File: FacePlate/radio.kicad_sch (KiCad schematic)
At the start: 4 parts, among them U3 SX1280

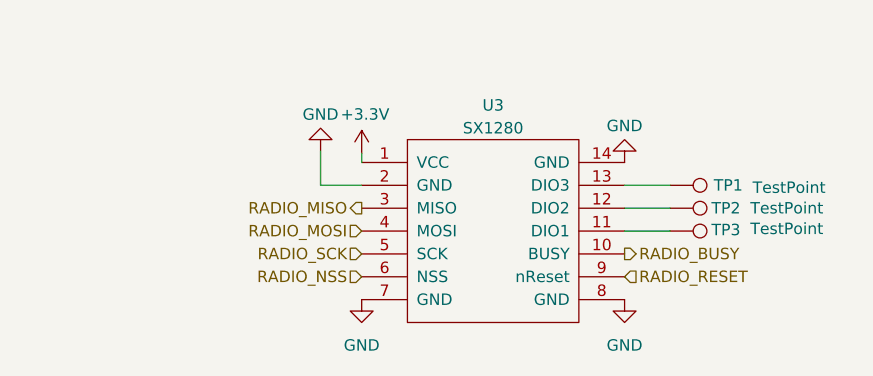
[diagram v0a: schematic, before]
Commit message: WIP Buck for Faceplate
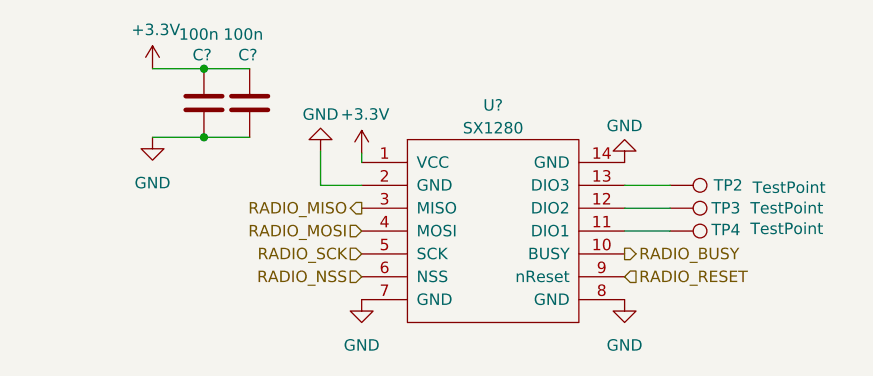
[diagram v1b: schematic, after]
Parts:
- added C? (x2): 100n, Capacitor_SMD:C_0603_1608Metric, symbol Device:C
- TP2: renamed from TP1; footprint (none) -> TestPoint:TestPoint_Pad_D1.0mm
- TP3: renamed from TP2; footprint (none) -> TestPoint:TestPoint_Pad_D1.0mm
- TP4: renamed from TP3; footprint (none) -> TestPoint:TestPoint_Pad_D1.0mm
- U?: renamed from U3; footprint BlueKitchen:E28-2G4M12S-SX1280 -> SX1280:E28-2G4M12S-SX1280
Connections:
- net +3.3V: now also C?.1, C?.1
- net GND: now also C?.2, C?.2

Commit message: Finalize faceplate
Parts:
- C?: LCSC C307341 -> C14663
- C?: LCSC C307340 -> C14663
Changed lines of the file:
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@@
       (effects (font (size 1.27 1.27)) hide)
     )
-    (property "LCSC" "C307341" (at 114.3 84.836 0)
+    (property "LCSC" "C14663" (at 114.3 84.836 0)
       (effects (font (size 1.27 1.27)) (justify left) hide)
     )
@@
       (effects (font (size 1.27 1.27)) hide)
     )
-    (property "LCSC" "C307340" (at 109.22 84.836 0)
+    (property "LCSC" "C14663" (at 109.22 84.836 0)
       (effects (font (size 1.27 1.27)) (justify left) hide)
     )

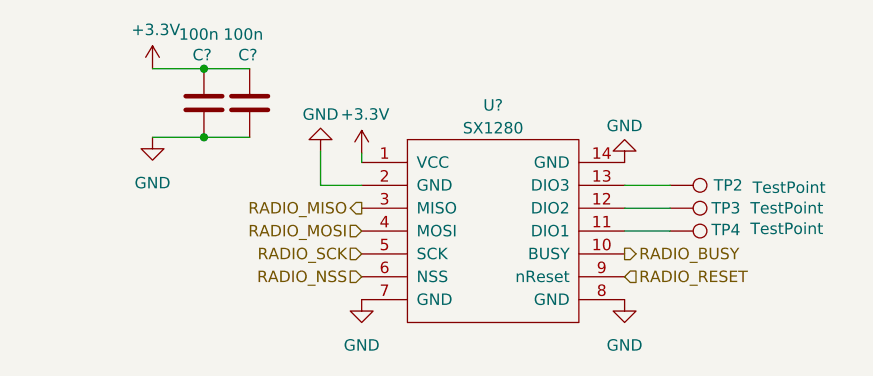
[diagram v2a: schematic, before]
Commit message: finalize with 0ohms
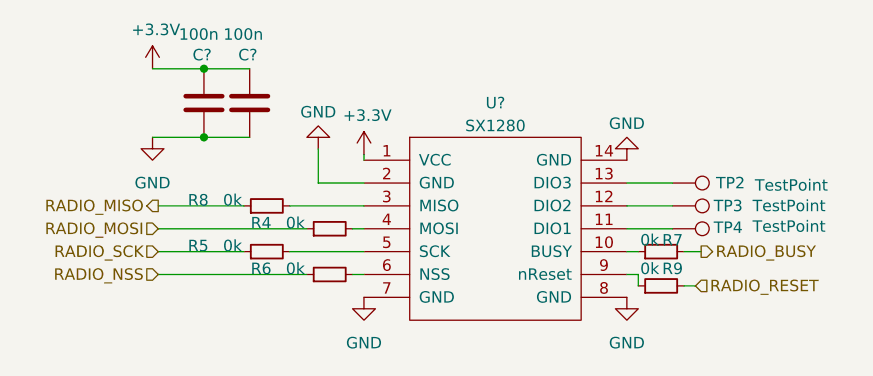
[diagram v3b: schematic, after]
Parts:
- added R4, R5, R6, R7, R8, R9: 0k, Resistor_SMD:R_0603_1608Metric, symbol Device:R_Small
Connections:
- net RADIO_BUSY: now also R7.2; no longer U?.10 (BUSY)
- net RADIO_MISO: now also R8.1; no longer U?.3 (MISO)
- net RADIO_MOSI: now also R4.1; no longer U?.4 (MOSI)
- net RADIO_NSS: now also R6.1; no longer U?.6 (NSS)
- net RADIO_RESET: now also R9.2; no longer U?.9 (nReset)
- net RADIO_SCK: now also R5.1; no longer U?.5 (SCK)
- new net: R4.2, U?.4 (MOSI)
- new net: R7.1, U?.10 (BUSY)
- new net: R8.2, U?.3 (MISO)
- new net: R5.2, U?.5 (SCK)
- new net: R6.2, U?.6 (NSS)
- new net: R9.1, U?.9 (nReset)

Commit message: faceplate updates
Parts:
- removed C? (x2): 100n, Capacitor_SMD:C_0603_1608Metric, symbol Device:C
- added C8 (x2): 0.1u, bots:C_0603_1608Metric, symbol bots:C_0.1u
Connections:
- net +3.3V: now also C8.1, C8.1
- net GND: now also C8.2, C8.2
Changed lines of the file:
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@@
 (kicad_sch (version 20230121) (generator eeschema)
   (paper "A4")
-  (junction (at 110.49 83.82) (diameter 0) (color 0 0 0 0)
-  )
-  (junction (at 110.49 76.2) (diameter 0) (color 0 0 0 0)
+  (junction (at 107.95 83.82) (diameter 0) (color 0 0 0 0)
+  )
+  (junction (at 107.95 76.2) (diameter 0) (color 0 0 0 0)
+  )
+  (wire (pts (xy 107.95 76.2) (xy 115.57 76.2))
+    (stroke (width 0) (type default))
+  )
+  (wire (pts (xy 107.95 83.82) (xy 115.57 83.82))
+    (stroke (width 0) (type default))
   )
   (wire (pts (xy 123.19 85.09) (xy 123.19 88.9))
     (stroke (width 0) (type default))
   )
-  (wire (pts (xy 104.775 76.2) (xy 110.49 76.2))
+  (wire (pts (xy 104.775 76.2) (xy 107.95 76.2))
     (stroke (width 0) (type default))
   )
@@
     (stroke (width 0) (type default))
   )
-  (wire (pts (xy 110.49 76.2) (xy 115.57 76.2))
-    (stroke (width 0) (type default))
-  )
   (wire (pts (xy 120.015 96.52) (xy 128.27 96.52))
     (stroke (width 0) (type default))
@@
     (stroke (width 0) (type default))
   )
-  (wire (pts (xy 104.775 83.82) (xy 110.49 83.82))
-    (stroke (width 0) (type default))
-  )
   (wire (pts (xy 158.75 99.06) (xy 157.48 99.06))
     (stroke (width 0) (type default))
@@
     (stroke (width 0) (type default))
   )
-  (wire (pts (xy 110.49 83.82) (xy 115.57 83.82))
+  (wire (pts (xy 104.775 83.82) (xy 107.95 83.82))
     (stroke (width 0) (type default))
   )
@@
   (hierarchical_label "RADIO_RESET" (shape input) (at 165.1 100.33 0) (fields_autoplaced)
     (effects (font (size 1.27 1.27)) (justify left))
+  )
+  (symbol (lib_id "bots:C_0.1u") (at 107.95 80.01 0) (unit 1)
+    (in_bom yes) (on_board yes) (dnp no) (fields_autoplaced)
+    (property "Reference" "C8" (at 111.76 78.74 0)
+      (effects (font (size 1.27 1.27)) (justify left))
+    )
+    (property "Value" "0.1u" (at 111.76 81.28 0)
+      (effects (font (size 1.27 1.27)) (justify left))
+    )
+    (property "Footprint" "bots:C_0603_1608Metric" (at 108.9152 83.82 0)
+      (effects (font (size 1.27 1.27)) hide)
+    )
+    (property "Datasheet" "~" (at 107.95 80.01 0)
+      (effects (font (size 1.27 1.27)) hide)
+    )
+    (pin "1")
+    (pin "2")
+    (instances
+      (project "FacePlate"
+        (path "/e63e39d7-6ac0-4ffd-8aa3-1841a4541b55/99bd3b0c-5cef-43ec-97f5-6b19c715565b"
+          (reference "C8") (unit 1)
+        )
+        (path "/e63e39d7-6ac0-4ffd-8aa3-1841a4541b55/e8e72004-885a-48f0-be5d-3ccbb5e9b4ac"
+          (reference "C11") (unit 1)
+        )
+      )
+    )
   )
   (symbol (lib_id "power:GND") (at 128.27 101.6 0) (unit 1)
@@
     )
   )
-  (symbol (lib_id "Device:C") (at 115.57 80.01 0) (unit 1)
-    (in_bom yes) (on_board yes) (dnp no)
-    (property "Reference" "C?" (at 114.3 74.676 0)
-      (effects (font (size 1.27 1.27)) (justify left))
-    )
-    (property "Value" "100n" (at 112.649 72.39 0)
-      (effects (font (size 1.27 1.27)) (justify left))
-    )
-    (property "Footprint" "Capacitor_SMD:C_0603_1608Metric" (at 116.5352 83.82 0)
+  (symbol (lib_id "bots:C_0.1u") (at 115.57 80.01 0) (unit 1)
+    (in_bom yes) (on_board yes) (dnp no) (fields_autoplaced)
+    (property "Reference" "C8" (at 119.38 78.74 0)
+      (effects (font (size 1.27 1.27)) (justify left))
+    )
+    (property "Value" "0.1u" (at 119.38 81.28 0)
+      (effects (font (size 1.27 1.27)) (justify left))
+    )
+    (property "Footprint" "bots:C_0603_1608Metric" (at 116.5352 83.82 0)
       (effects (font (size 1.27 1.27)) hide)
     )
@@
       (effects (font (size 1.27 1.27)) hide)
     )
-    (property "LCSC" "C14663" (at 114.3 84.836 0)
-      (effects (font (size 1.27 1.27)) (justify left) hide)
-    )
-    (pin "1")
-    (pin "2")
-    (instances
-      (project "BoardyMcBoardFace"
-        (path "/ce9c697a-7c8e-40f4-9393-5cd88edd7734"
-          (reference "C?") (unit 1)
-        )
-      )
-      (project "FacePlate"
-        (path "/e63e39d7-6ac0-4ffd-8aa3-1841a4541b55"
-          (reference "C?") (unit 1)
-        )
-        (path "/e63e39d7-6ac0-4ffd-8aa3-1841a4541b55/e8e72004-885a-48f0-be5d-3ccbb5e9b4ac"
-          (reference "C11") (unit 1)
+    (pin "1")
+    (pin "2")
+    (instances
+      (project "FacePlate"
+        (path "/e63e39d7-6ac0-4ffd-8aa3-1841a4541b55/99bd3b0c-5cef-43ec-97f5-6b19c715565b"
+          (reference "C8") (unit 1)
+        )
+        (path "/e63e39d7-6ac0-4ffd-8aa3-1841a4541b55/e8e72004-885a-48f0-be5d-3ccbb5e9b4ac"
+          (reference "C10") (unit 1)
         )
       )
@@
         )
       )
-    )
-  )
-  (symbol (lib_id "Device:C") (at 110.49 80.01 0) (unit 1)
-    (in_bom yes) (on_board yes) (dnp no)
-    (property "Reference" "C?" (at 109.22 74.676 0)
-      (effects (font (size 1.27 1.27)) (justify left))
-    )
-    (property "Value" "100n" (at 107.696 72.39 0)
-      (effects (font (size 1.27 1.27)) (justify left))
-    )
-    (property "Footprint" "Capacitor_SMD:C_0603_1608Metric" (at 111.4552 83.82 0)
-      (effects (font (size 1.27 1.27)) hide)
-    )
-    (property "Datasheet" "~" (at 110.49 80.01 0)
-      (effects (font (size 1.27 1.27)) hide)
-    )
-    (property "LCSC" "C14663" (at 109.22 84.836 0)
-      (effects (font (size 1.27 1.27)) (justify left) hide)
-    )
-    (pin "1")
-    (pin "2")
-    (instances
-      (project "BoardyMcBoardFace"
-        (path "/ce9c697a-7c8e-40f4-9393-5cd88edd7734"
-          (reference "C?") (unit 1)
-        )
-      )
-      (project "FacePlate"
-        (path "/e63e39d7-6ac0-4ffd-8aa3-1841a4541b55"
-          (reference "C?") (unit 1)
-        )
-        (path "/e63e39d7-6ac0-4ffd-8aa3-1841a4541b55/e8e72004-885a-48f0-be5d-3ccbb5e9b4ac"
-          (reference "C10") (unit 1)
-        )
-      )

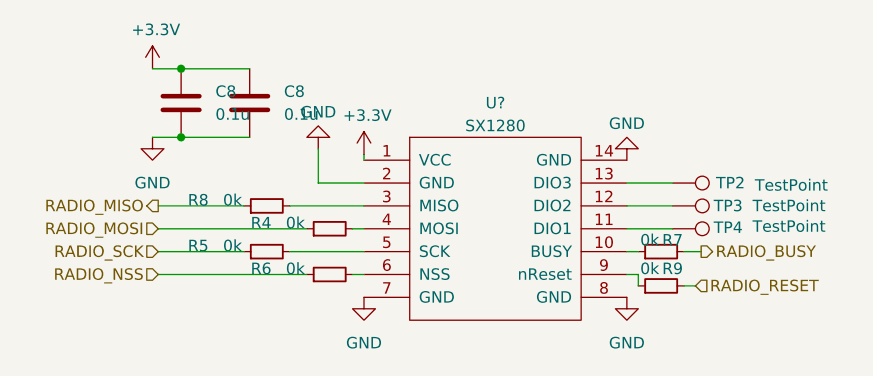
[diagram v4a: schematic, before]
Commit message: faceplate radio fixes
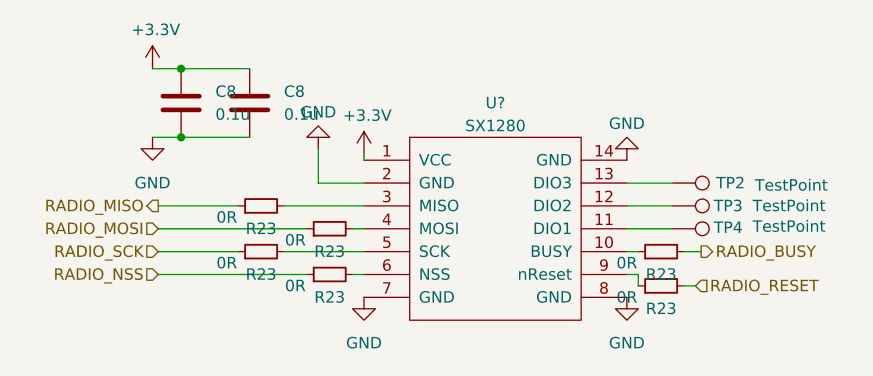
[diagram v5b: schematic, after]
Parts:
- removed R4, R5, R6, R7, R8, R9: 0k, Resistor_SMD:R_0603_1608Metric, symbol Device:R_Small
- added R23 (x6): 0R, bots:R_0603_1608Metric, symbol bots:0R
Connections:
- net RADIO_BUSY: now also R23.2
- net RADIO_MISO: now also R23.1
- net RADIO_MOSI: now also R23.1
- net RADIO_NSS: now also R23.1
- net RADIO_RESET: now also R23.2
- net RADIO_SCK: now also R23.1
- net at U?.4 (MOSI): now also R23.2
- net at U?.10 (BUSY): now also R23.1
- net at U?.3 (MISO): now also R23.2
- net at U?.5 (SCK): now also R23.2
- net at U?.6 (NSS): now also R23.2
- net at U?.9 (nReset): now also R23.1

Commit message: Ordered faceplate
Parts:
- C8: value 0.1u -> 100n; footprint bots:C_0603_1608Metric -> bots:C_0402_1005Metric; LCSC (none) -> C307331
- R23: LCSC (none) -> C21189
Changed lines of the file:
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@@
       (effects (font (size 1.27 1.27)) (justify left))
     )
-    (property "Value" "0.1u" (at 111.76 81.28 0)
-      (effects (font (size 1.27 1.27)) (justify left))
-    )
-    (property "Footprint" "bots:C_0603_1608Metric" (at 108.9152 83.82 0)
+    (property "Value" "100n" (at 111.76 81.28 0)
+      (effects (font (size 1.27 1.27)) (justify left))
+    )
+    (property "Footprint" "bots:C_0402_1005Metric" (at 108.9152 83.82 0)
       (effects (font (size 1.27 1.27)) hide)
     )
     (property "Datasheet" "~" (at 107.95 80.01 0)
+      (effects (font (size 1.27 1.27)) hide)
+    )
+    (property "LCSC" "C307331" (at 107.95 80.01 0)
       (effects (font (size 1.27 1.27)) hide)
     )
@@
       (effects (font (size 1.27 1.27)) hide)
     )
+    (property "LCSC" "C21189" (at 116.84 91.44 0)
+      (effects (font (size 1.27 1.27)) hide)
+    )
     (pin "1")
     (pin "2")
@@
     )
     (property "Datasheet" "~" (at 116.84 96.52 0)
+      (effects (font (size 1.27 1.27)) hide)
+    )
+    (property "LCSC" "C21189" (at 116.84 96.52 0)
       (effects (font (size 1.27 1.27)) hide)
     )
@@
       (effects (font (size 1.27 1.27)) hide)
     )
+    (property "LCSC" "C21189" (at 161.29 96.52 0)
+      (effects (font (size 1.27 1.27)) hide)
+    )
     (pin "1")
     (pin "2")
@@
       (effects (font (size 1.27 1.27)) hide)
     )
+    (property "LCSC" "C21189" (at 161.29 100.33 0)
+      (effects (font (size 1.27 1.27)) hide)
+    )
     (pin "1")
     (pin "2")
@@
       (effects (font (size 1.27 1.27)) hide)
     )
+    (property "LCSC" "C21189" (at 124.46 93.98 0)
+      (effects (font (size 1.27 1.27)) hide)
+    )
     (pin "1")
     (pin "2")
@@
       (effects (font (size 1.27 1.27)) (justify left))
     )
-    (property "Value" "0.1u" (at 119.38 81.28 0)
-      (effects (font (size 1.27 1.27)) (justify left))
-    )
-    (property "Footprint" "bots:C_0603_1608Metric" (at 116.5352 83.82 0)
+    (property "Value" "100n" (at 119.38 81.28 0)
+      (effects (font (size 1.27 1.27)) (justify left))
+    )
+    (property "Footprint" "bots:C_0402_1005Metric" (at 116.5352 83.82 0)
       (effects (font (size 1.27 1.27)) hide)
     )
     (property "Datasheet" "~" (at 115.57 80.01 0)
+      (effects (font (size 1.27 1.27)) hide)
+    )
+    (property "LCSC" "C307331" (at 115.57 80.01 0)
       (effects (font (size 1.27 1.27)) hide)
     )
@@
       (effects (font (size 1.27 1.27)) hide)
     )
+    (property "LCSC" "C21189" (at 124.46 99.06 0)
+      (effects (font (size 1.27 1.27)) hide)
+    )

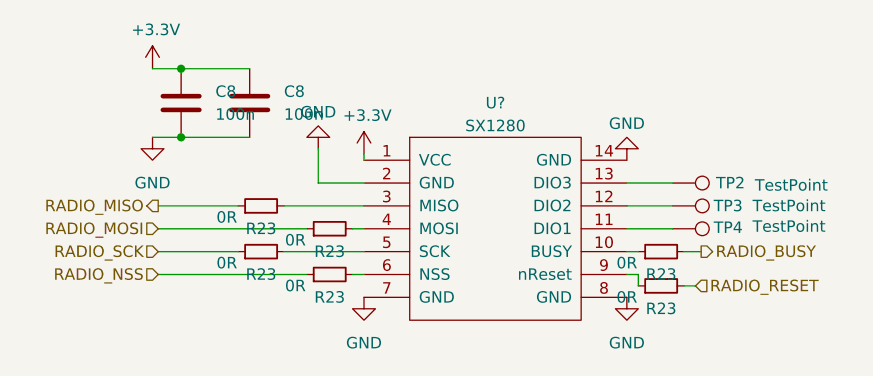
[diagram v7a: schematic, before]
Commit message: changed transceiver for faceplate
+ removed caps on chicker can
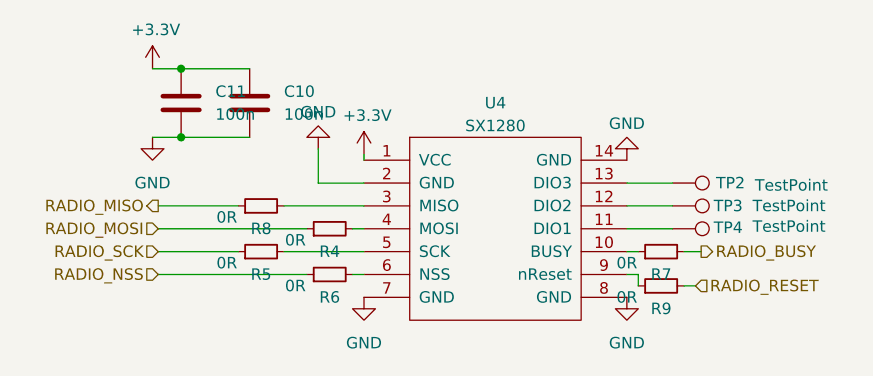
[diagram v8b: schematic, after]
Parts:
- gave numbers to parts that had none: 1
- renumbered C8 to C10, C8 to C11, R23 to R4, R23 to R5, R23 to R6, R23 to R7, R23 to R8, R23 to R9
